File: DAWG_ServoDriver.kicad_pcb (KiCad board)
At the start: 2 copper layers, 70 x 94.8 mm, 152 parts, among them CN10 Conn_02x19_Odd_Even, CN7 Conn_02x19_Odd_Even, IC1 DRV8251ADDAR, IC2 DRV8251ADDAR, IC3 DRV8251ADDAR, IC4 DRV8251ADDAR, IC5 ESP32-PICO-MINI-02-N8R2, J1 Screw_Terminal_01x06, J11 Conn_01x10, J12 Conn_01x08, J13 Screw_Terminal_01x06, J14 Conn_01x06, J15 Conn_01x08, J17 Conn_01x03, J18 Conn_01x03, J19 Conn_01x03, J20 Conn_01x03, J21 Conn_01x03, J22 Conn_01x03, J23 Conn_01x03, J24 Conn_01x03, J25 Conn_01x03, J26 Conn_01x03, J27 Conn_01x03, J28 Conn_01x03, J29 Conn_01x03, J3 Screw_Terminal_01x06, J30 Conn_01x03, J31 Conn_01x03, J32 Conn_01x03, J33 Conn_01x03, J34 Conn_01x03, J35 Conn_01x03, J36 Conn_01x03, J4 Conn_01x04_Pin, J6 Conn_01x03, J7 Screw_Terminal_01x02, J8 Screw_Terminal_01x02, J9 Screw_Terminal_01x06, Q1 BSS138, Q10 BSS138, Q11 BSS138, Q12 BSS138, Q13 BSS138, Q14 BSS138, Q15 BSS138, Q16 BSS138, Q17 BSS138, Q18 BSS138, Q19 BSS138, Q2 BSS138, Q20 BSS138, Q3 BSS138, Q4 BSS138, Q5 BSS138, Q6 BSS138, Q7 BSS138, Q8 BSS138, Q9 BSS138, SW1 SW_Push, U1 TPS62177DQC, U2 STM32G431C8Tx, U3 LD1117S12TR_SOT223, U4 ICM-20602, U5 ICM-20602, Y1 Crystal_GND24

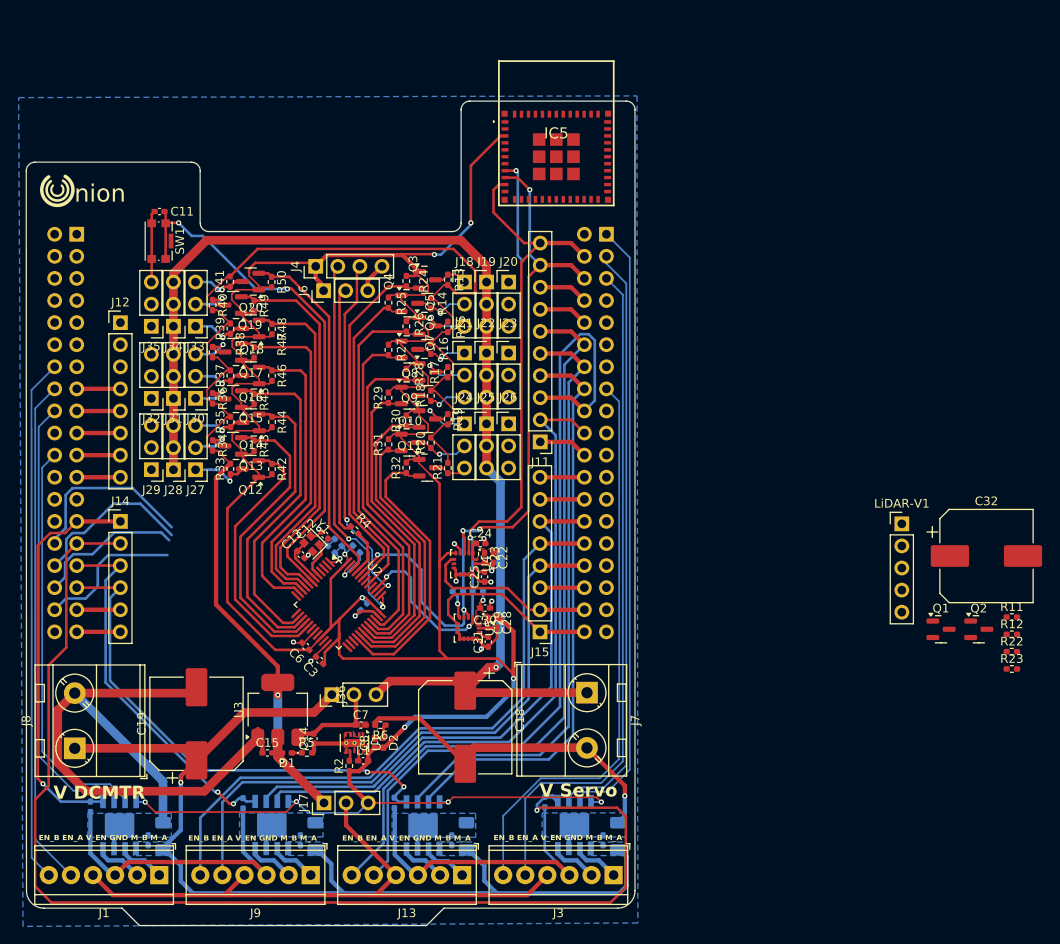
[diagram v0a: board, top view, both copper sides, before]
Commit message: added esp32 & lidar, finished routing unrouted stuff
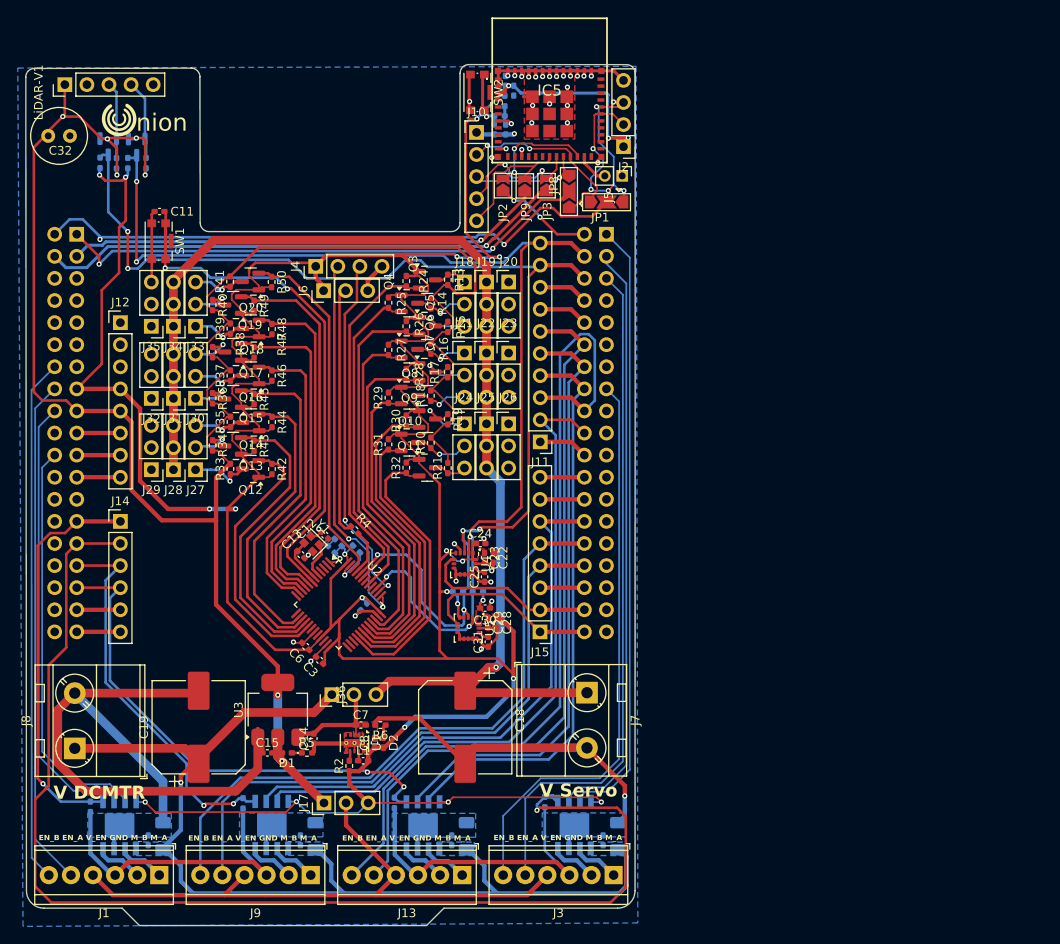
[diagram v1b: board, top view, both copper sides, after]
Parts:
- added C33: 100n, Capacitor_SMD:C_0402_1005Metric_Pad0.74x0.62mm_HandSolder, B.Cu at (79.1, 65.8)
- added C34: 22u, Capacitor_SMD:C_0402_1005Metric_Pad0.74x0.62mm_HandSolder, B.Cu at (78.2, 64.7)
- added C35: 1u, Capacitor_SMD:C_0402_1005Metric_Pad0.74x0.62mm_HandSolder, B.Cu at (78.2, 70.3)
- added C36: 0.1u, Capacitor_SMD:C_0402_1005Metric_Pad0.74x0.62mm_HandSolder, B.Cu at (76.9, 70.3)
- added J10: Conn_01x05_Pin, Connector_PinHeader_2.54mm:PinHeader_1x05_P2.54mm_Vertical, F.Cu at (74.8, 70.6)
- added J2: Conn_01x04_Pin, Connector_PinHeader_2.54mm:PinHeader_1x04_P2.54mm_Vertical, F.Cu at (91.8, 72.2)
- added J5: Conn_01x02_Pin, Connector_PinHeader_2.00mm:PinHeader_1x02_P2.00mm_Vertical, F.Cu at (91.6, 75.6)
- added JP1: SolderJumper_3_Open, Jumper:SolderJumper-3_P2.0mm_Open_TrianglePad1.0x1.5mm, F.Cu at (89.8, 78.6)
- added JP2: SolderJumper_2_Open, Jumper:SolderJumper-2_P1.3mm_Open_TrianglePad1.0x1.5mm, F.Cu at (77.9, 76.7)
- added JP3: SolderJumper_2_Open, Jumper:SolderJumper-2_P1.3mm_Open_TrianglePad1.0x1.5mm, F.Cu at (82.9, 76.7)
- added JP8: SolderJumper_3_Open, Jumper:SolderJumper-3_P2.0mm_Open_TrianglePad1.0x1.5mm, F.Cu at (85.5, 77.4)
- added JP9: SolderJumper_2_Open, Jumper:SolderJumper-2_P1.3mm_Open_TrianglePad1.0x1.5mm, F.Cu at (80.4, 76.8)
- added R51: 10k, Resistor_SMD:R_0402_1005Metric_Pad0.72x0.64mm_HandSolder, B.Cu at (78.1, 67.0)
- added R52: 0, Resistor_SMD:R_0402_1005Metric_Pad0.72x0.64mm_HandSolder, B.Cu at (77.5, 68.7)
- added SW2: SW_Push, Button_Switch_SMD:SW_Push_1P1T-SH_NO_CK_KMR2xxG, F.Cu at (75.0, 66.0)
- C32: value 680u -> 470u; footprint Capacitor_SMD:CP_Elec_10x10.5 -> Capacitor_THT:C_Radial_D6.3mm_H7.0mm_P2.50mm
- IC5: footprint Package_DFN_QFN:ESP32PICOMINI02N8R2 -> ESP32-PICO-MINI-02-N8R2:ESP32PICOMINI02N8R2
- Q1, Q2, R11, R12, R22, R23: moved to B.Cu
- moved C32 118.2 mm to (25.6, 71.0)
- moved R22 117.3 mm to (33.5, 74.2), turned to -90 degrees
- moved R11 117.1 mm to (31.6, 74.1), turned to -90 degrees
- moved R23 115.3 mm to (36.9, 74.1), turned to -90 degrees
- moved R12 115.2 mm to (34.8, 74.1), turned to -90 degrees
- moved Q2 111.6 mm to (35.8, 72.3), turned to -90 degrees
- moved Q1 110.7 mm to (32.5, 72.2), turned to -90 degrees
- moved LiDAR-V1 108.7 mm to (27.5, 65.1), turned to 90 degrees
- moved IC5 4.99 mm to (83.2, 68.5)
- moved C19 0.47 mm to (42.9, 139.0)
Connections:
- CN10 pad 2: unconnected-(CN10-Pin_2-Pad2) -> /HANDSHAKE_STM32
- CN7 pad 1: unconnected-(CN7-Pin_1-Pad1) -> /MISO3/RX3
- CN7 pad 2: unconnected-(CN7-Pin_2-Pad2) -> /SCK3/TX3
- CN7 pad 3: unconnected-(CN7-Pin_3-Pad3) -> /ESP32_CS
- CN7 pad 4: unconnected-(CN7-Pin_4-Pad4) -> /MOSI3
- IC5 pad 10: /I2C1_SCL -> unconnected-(IC5-I35-Pad10)
- IC5 pad 18: unconnected-(IC5-IO14-Pad18) -> /TMS
- IC5 pad 19: unconnected-(IC5-IO12-Pad19) -> /TDI
- IC5 pad 20: unconnected-(IC5-IO13-Pad20) -> /TCK
- IC5 pad 21: unconnected-(IC5-IO15-Pad21) -> /TDO
- IC5 pad 22: unconnected-(IC5-IO2-Pad22) -> /HANDSHAKE_ESP32
- IC5 pad 23: unconnected-(IC5-IO0-Pad23) -> /BOOT0_ESP32
- IC5 pad 30: unconnected-(IC5-RXD0-Pad30) -> /ESP_RX
- IC5 pad 31: unconnected-(IC5-TXD0-Pad31) -> /ESP_TX
- IC5 pad 9: /I2C1_SDA -> unconnected-(IC5-I34-Pad9)
- R4 pad 2: /BOOT0 -> /BOOT0_STM32
- U2 pad 45: /BOOT0 -> /BOOT0_STM32
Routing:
- net +3.3V: track 377.4 -> 478.9 mm, vias 13 -> 24
- net +5V: track 154.9 -> 242.2 mm, vias 2 -> 7
- net /SCK3/TX3: track 0.00 -> 68.8 mm, vias 0 -> 2
- net /MISO3/RX3: track 0.00 -> 62.1 mm, vias 0 -> 2
- net /MOSI3: track 0.00 -> 60.7 mm, vias 0 -> 1
- net /ESP32_CS: track 0.00 -> 55.0 mm, vias 0 -> 1
- net /I2C1_SDA: track 88.8 -> 141.6 mm, vias 5 -> 6
- net /I2C1_SCL: track 85.6 -> 136.9 mm, vias 3 -> 5
- net GND: track 269.5 -> 316.9 mm, vias 14 -> 39
- net /ESP_RX: track 0.00 -> 20.6 mm, vias 0 -> 3
- net unconnected-(CN7-Pin_30-Pad30): track 20.5 -> 0.51 mm
- net /TDO: track 0.00 -> 19.6 mm, vias 0 -> 2
- net unconnected-(CN7-Pin_32-Pad32): track 18.9 -> 0.00 mm
- net /ESP_TX: track 0.00 -> 17.2 mm, vias 0 -> 3
- net unconnected-(CN7-Pin_34-Pad34): track 17.2 -> 0.00 mm
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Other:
- board size 70 x 94.8 mm -> 70.1 x 99 mm

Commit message: added selectable I2C/UART for peripheral (LIDAR), added some annotation for soldermaks
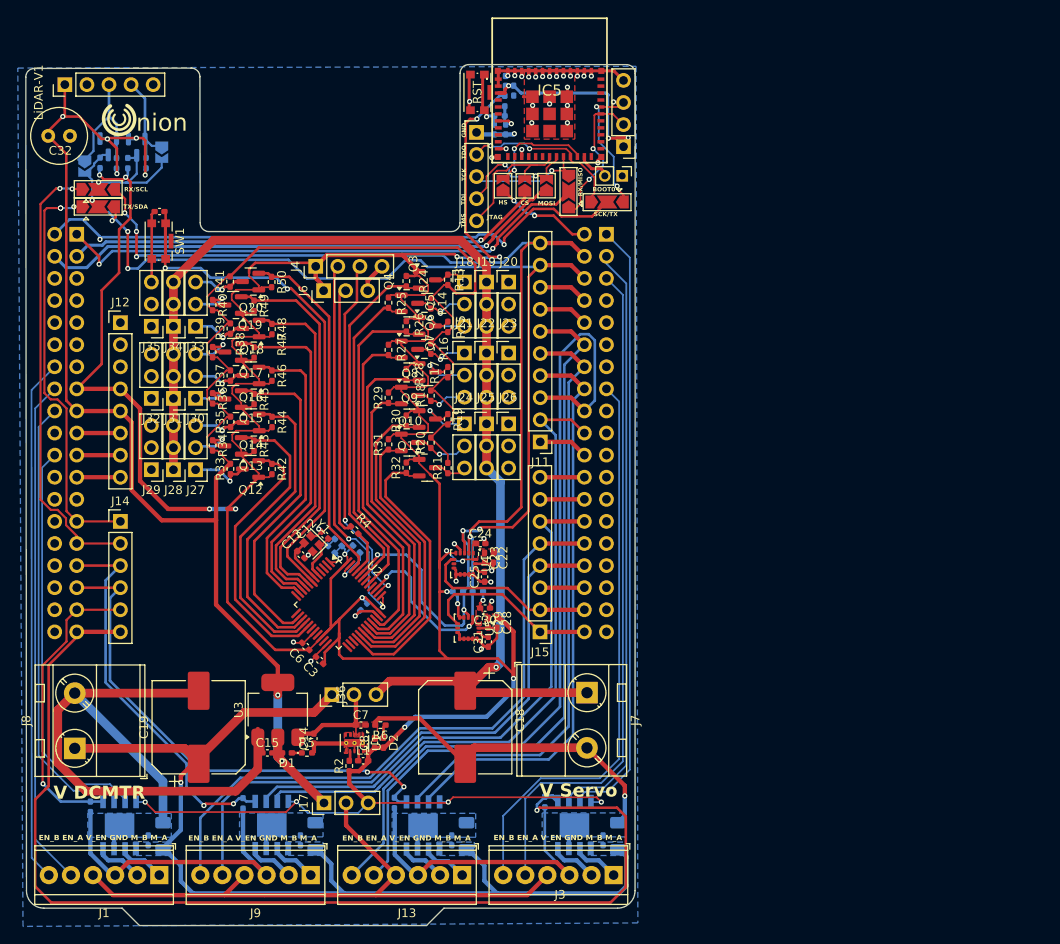
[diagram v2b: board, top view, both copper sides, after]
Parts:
- added RX/SCL: SolderJumper_3_Open, Jumper:SolderJumper-3_P2.0mm_Open_TrianglePad1.0x1.5mm, F.Cu at (31.4, 77.2)
- added SHORT: SolderJumper_2_Open, Jumper:SolderJumper-2_P1.3mm_Open_TrianglePad1.0x1.5mm, B.Cu at (29.8, 74.5)
- added SHORT: SolderJumper_2_Open, Jumper:SolderJumper-2_P1.3mm_Open_TrianglePad1.0x1.5mm, B.Cu at (38.6, 72.9)
- added TX/SDA: SolderJumper_3_Open, Jumper:SolderJumper-3_P2.0mm_Open_TrianglePad1.0x1.5mm, F.Cu at (31.4, 79.2)
- moved SCK/TX 0.06 mm to (89.9, 78.6)
- renumbered J5 to BOOT0, JP9 to CS, JP2 to HS, J10 to JTAG, JP3 to MOSI, SW2 to RST, JP8 to RX/MISO, JP1 to SCK/TX
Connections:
- CN7 pad 27: /IsenseM1 -> /UART4_TX
- CN7 pad 29: /IsenseM2 -> /UART4_RX
- CN7 pad 35: Net-(CN7-Pin_35) -> /IsenseM1
- CN7 pad 37: Net-(CN7-Pin_37) -> /IsenseM2
- J14 pad 1: /IsenseM1 -> /UART4_TX
- J14 pad 2: /IsenseM2 -> /UART4_RX
- J14 pad 5: Net-(CN7-Pin_35) -> /IsenseM1
- J14 pad 6: Net-(CN7-Pin_37) -> /IsenseM2
- Q1 pad 3: /I2C1_SDA -> /I2C1_SDA_SEL
- Q2 pad 3: /I2C1_SCL -> /I2C1_SCL_SEL
- R11 pad 1: /I2C1_SDA -> /I2C1_SDA_SEL
- R12 pad 1: /I2C1_SCL -> /I2C1_SCL_SEL
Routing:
- net /UART4_RX: track 0.00 -> 52.0 mm, vias 0 -> 2
- net /UART4_TX: track 0.00 -> 47.4 mm, vias 0 -> 3
- net /I2C1_SCL_SEL: track 0.00 -> 14.8 mm, vias 0 -> 1
- net /IsenseM1: track 46.0 -> 34.4 mm
- net /I2C1_SDA_5V: track 8.80 -> 19.4 mm
- net /IsenseM2: track 138.4 -> 128.2 mm
- net /I2C1_SDA_SEL: track 0.00 -> 8.25 mm, vias 0 -> 1
- net /I2C1_SDA: track 141.6 -> 136.2 mm, vias 6 -> 7
- net Net-(CN7-Pin_37): track 5.02 -> 0.00 mm
- net Net-(CN7-Pin_35): track 5.02 -> 0.00 mm
- net /I2C1_SCL: track 136.9 -> 132.1 mm, vias 5 -> 6
- net +5V: track 242.2 -> 238.5 mm
- net /ESP_RX: track 20.6 -> 17.7 mm, vias 3 -> 2
- net /I2C1_SCL_5V: track 9.17 -> 11.4 mm
- net /TDI: track 15.7 -> 14.9 mm
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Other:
- board text added: "GND"
- board text added: "TCK"
- board text added: "TDI"
- board text added: "TDO"
- board text added: "TMS"
